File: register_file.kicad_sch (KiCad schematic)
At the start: 6 parts, among them U1 74HC173, U2 74HC173, U3 74HC173, U4 74HC173, U5 74HC04

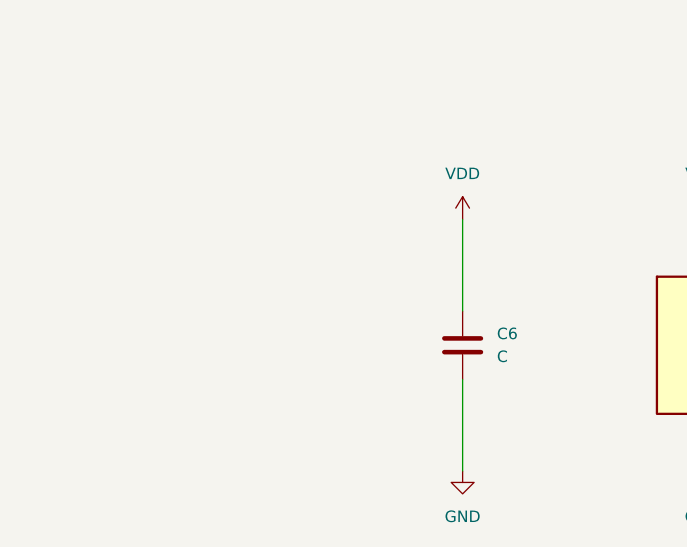
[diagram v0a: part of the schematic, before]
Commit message: fix: added missing register_file decoupling capacitors
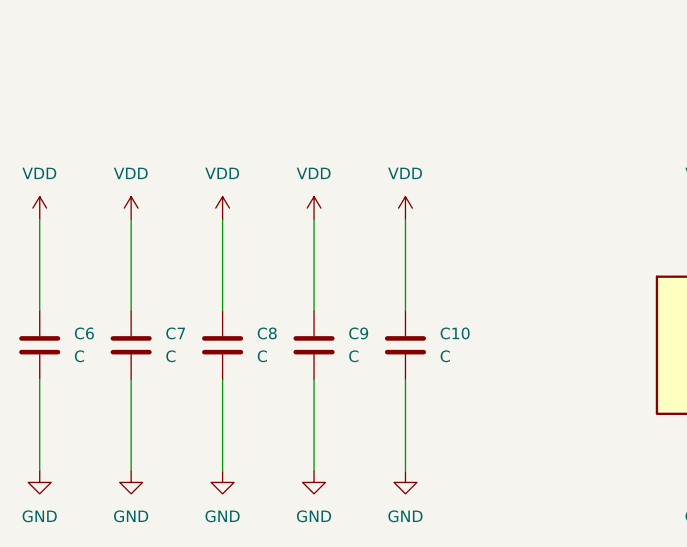
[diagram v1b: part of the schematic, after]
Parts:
- added C10, C7, C8, C9: C, symbol Device:C
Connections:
- net GND: now also C10.2, C7.2, C8.2, C9.2
- net VDD: now also C10.1, C7.1, C8.1, C9.1
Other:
- moved on the sheet: C6

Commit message: feat: pcb schematic finalization
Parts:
- C10, C6, C7, C8, C9: value C -> 100n; footprint (none) -> Capacitor_SMD:C_0603_1608Metric_Pad1.08x0.95mm_HandSolder
- U1, U2, U3, U4: footprint (none) -> Package_SO:TSSOP-16_4.4x5mm_P0.65mm
- U5: footprint (none) -> Package_SO:SOIC-14_3.9x8.7mm_P1.27mm
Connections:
- no-connect marks 2 -> 3
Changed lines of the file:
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@@
 	)
 	(no_connect
+		(at 88.9 57.15)
+	)
+	(no_connect
 		(at 158.75 165.1)
 	)
@@
 		)
 	)
+	(hierarchical_label "RST"
+		(shape input)
+		(at 88.9 57.15 180)
+		(effects
+			(font
+				(size 1.27 1.27)
+			)
+			(justify right)
+		)
+	)
 	(hierarchical_label "4_Q[3..0]"
 		(shape output)
@@
 			)
 		)
-		(property "Footprint" ""
+		(property "Footprint" "Package_SO:TSSOP-16_4.4x5mm_P0.65mm"
 			(at 127 60.96 0)
 			(hide yes)
@@
 			)
 		)
-		(property "Footprint" ""
+		(property "Footprint" "Package_SO:TSSOP-16_4.4x5mm_P0.65mm"
 			(at 127 124.46 0)
 			(hide yes)
@@
 			)
 		)
-		(property "Footprint" ""
+		(property "Footprint" "Package_SO:SOIC-14_3.9x8.7mm_P1.27mm"
 			(at 151.13 165.1 0)
 			(hide yes)
@@
 			)
 		)
-		(property "Value" "C"
+		(property "Value" "100n"
 			(at 36.83 175.2599 0)
 			(show_name no)
@@
 			)
 		)
-		(property "Footprint" ""
+		(property "Footprint" "Capacitor_SMD:C_0603_1608Metric_Pad1.08x0.95mm_HandSolder"
 			(at 33.9852 177.8 0)
 			(hide yes)
@@
 			)
 		)
-		(property "Footprint" ""
+		(property "Footprint" "Package_SO:SOIC-14_3.9x8.7mm_P1.27mm"
 			(at 102.87 129.54 0)
 			(hide yes)
@@
 			)
 		)
-		(property "Value" "C"
+		(property "Value" "100n"
 			(at 67.31 175.2599 0)
 			(show_name no)
@@
 			)
 		)
-		(property "Footprint" ""
+		(property "Footprint" "Capacitor_SMD:C_0603_1608Metric_Pad1.08x0.95mm_HandSolder"
 			(at 64.4652 177.8 0)
 			(hide yes)
@@
 			)
 		)
-		(property "Footprint" ""
+		(property "Footprint" "Package_SO:SOIC-14_3.9x8.7mm_P1.27mm"
 			(at 151.13 177.8 0)
 			(hide yes)
@@
 			)
 		)
-		(property "Footprint" ""
+		(property "Footprint" "Package_SO:SOIC-14_3.9x8.7mm_P1.27mm"
 			(at 153.67 66.04 0)
 			(hide yes)
@@
 			)
 		)
-		(property "Footprint" ""
+		(property "Footprint" "Package_SO:SOIC-14_3.9x8.7mm_P1.27mm"
 			(at 102.87 66.04 0)
 			(hide yes)
@@
 			)
 		)
-		(property "Footprint" ""
+		(property "Footprint" "Package_SO:TSSOP-16_4.4x5mm_P0.65mm"
 			(at 177.8 124.46 0)
 			(hide yes)
@@
 			)
 		)
-		(property "Footprint" ""
+		(property "Footprint" "Package_SO:TSSOP-16_4.4x5mm_P0.65mm"
 			(at 177.8 60.96 0)
 			(hide yes)
@@
 			)
 		)
-		(property "Value" "C"
+		(property "Value" "100n"
 			(at 26.67 175.2599 0)
 			(show_name no)
@@
 			)
 		)
-		(property "Footprint" ""
+		(property "Footprint" "Capacitor_SMD:C_0603_1608Metric_Pad1.08x0.95mm_HandSolder"
 			(at 23.8252 177.8 0)
 			(hide yes)
@@
 			)
 		)
-		(property "Footprint" ""
+		(property "Footprint" "Package_SO:SOIC-14_3.9x8.7mm_P1.27mm"
 			(at 153.67 129.54 0)
 			(hide yes)
@@
 			)
 		)
-		(property "Value" "C"
+		(property "Value" "100n"
 			(at 57.15 175.2599 0)
 			(show_name no)
@@
 			)
 		)
-		(property "Footprint" ""
+		(property "Footprint" "Capacitor_SMD:C_0603_1608Metric_Pad1.08x0.95mm_HandSolder"
 			(at 54.3052 177.8 0)
 			(hide yes)
@@
 			)
 		)
-		(property "Value" "C"
+		(property "Value" "100n"
 			(at 46.99 175.2599 0)
 			(show_name no)
@@
 			)
 		)
-		(property "Footprint" ""
+		(property "Footprint" "Capacitor_SMD:C_0603_1608Metric_Pad1.08x0.95mm_HandSolder"
 			(at 44.1452 177.8 0)
 			(hide yes)
@@
 			)
 		)
-		(property "Footprint" ""
+		(property "Footprint" "Package_SO:SOIC-14_3.9x8.7mm_P1.27mm"
 			(at 96.52 173.99 0)
 			(hide yes)
